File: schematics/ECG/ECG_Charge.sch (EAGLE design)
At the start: 8 parts, among them IC1 MCP73832_SOT23-5, J1 USB_MICROC

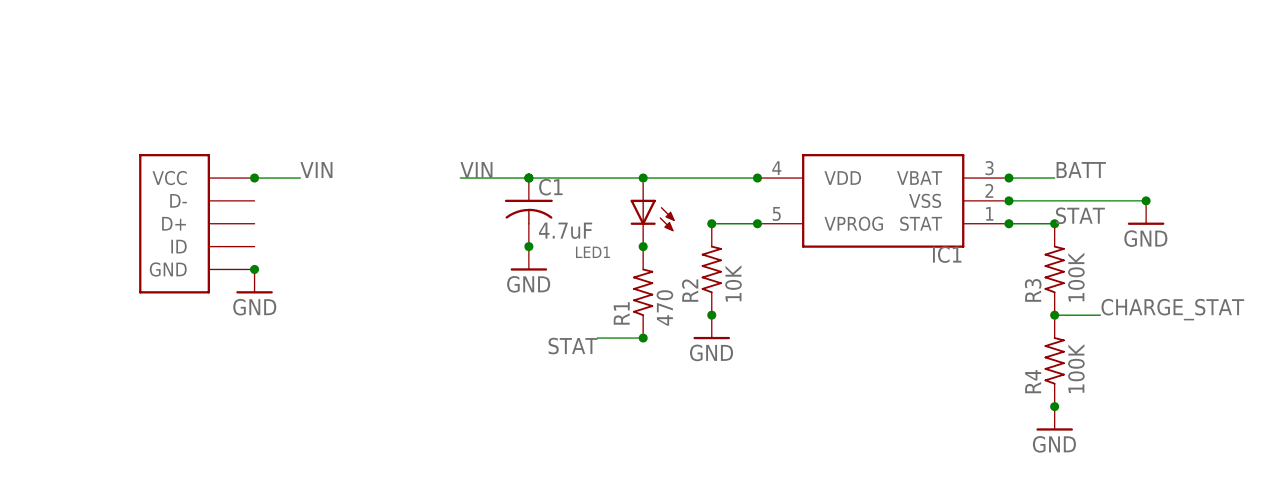
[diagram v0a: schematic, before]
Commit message: changed usb to micro usb, placed components in board area
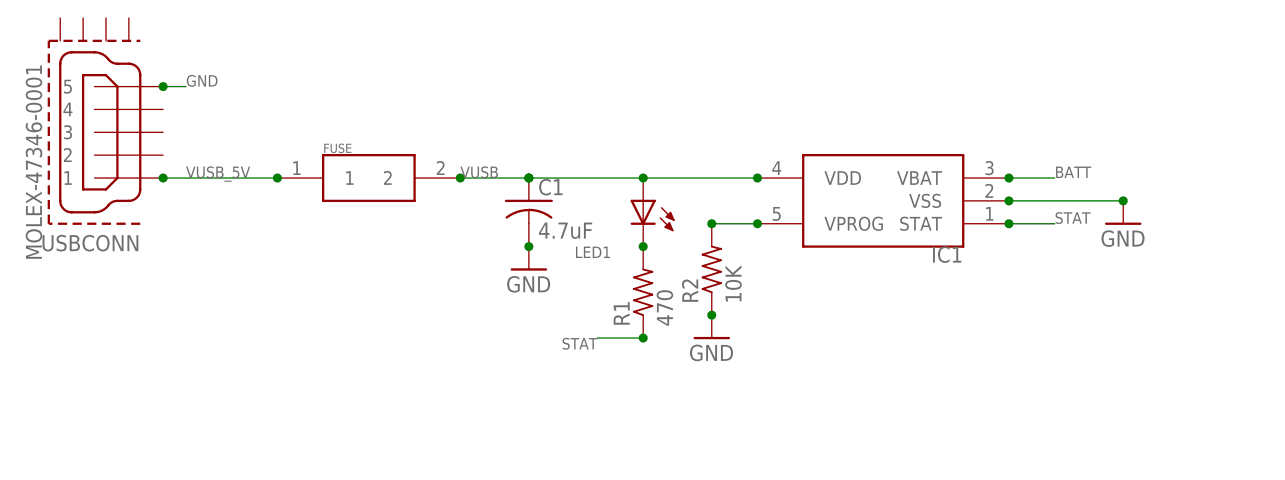
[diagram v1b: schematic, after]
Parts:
- removed J1: USB_MICROC, KomodoOpenLab:USB_MICROC
- removed R3, R4: 100K, rcl:R-US_R0201
- added FUSE: FUSE-MF_SERIES, bourns-fuse:FUSE-MF_SERIES
- added USBCONN: MOLEX-47346-0001, usb_con-update:MOLEX-47346-0001
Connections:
- removed net CHARGE_STAT: R3.1, R4.2
- removed net VIN: C1.1, IC1.VDD, J1.VCC, LED1.A
- new net VUSB: C1.1, FUSE.2, IC1.VDD, LED1.A
- new net VUSB_5V: FUSE.1, USBCONN.1
- net GND: now also USBCONN.5; no longer J1.GND, R4.1
- net STAT: no longer R3.2
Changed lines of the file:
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@@
 <parts>
 <part name="FRAME1" library="frames" deviceset="FRAME_A_L" device=""/>
-<part name="J1" library="KomodoOpenLab" deviceset="USB_MICROC" device=""/>
 <part name="IC1" library="KomodoOpenLab" deviceset="MCP73832_SOT23-5" device=""/>
 <part name="GND2" library="supply1" deviceset="GND" device=""/>
 <part name="R2" library="rcl" deviceset="R-US_" device="R0201" value="10K"/>
 <part name="GND3" library="supply1" deviceset="GND" device=""/>
-<part name="GND13" library="supply1" deviceset="GND" device=""/>
 <part name="C1" library="rcl" deviceset="C-US" device="C0402" value="4.7uF"/>
 <part name="GND19" library="supply1" deviceset="GND" device=""/>
-<part name="R3" library="rcl" deviceset="R-US_" device="R0201" value="100K"/>
-<part name="R4" library="rcl" deviceset="R-US_" device="R0201" value="100K"/>
-<part name="GND20" library="supply1" deviceset="GND" device=""/>
 <part name="LED1" library="LITEON" deviceset="LED_SMT_0805" device=""/>
 <part name="R1" library="rcl" deviceset="R-US_" device="R0201" value="470"/>
+<part name="USBCONN" library="usb_con-update" deviceset="MOLEX-47346-0001" device=""/>
+<part name="FUSE" library="bourns-fuse" deviceset="FUSE-MF_SERIES" device=""/>
 </parts>
 <sheets>
@@
 <instance part="FRAME1" gate="G$1" x="0" y="0"/>
 <instance part="FRAME1" gate="G$2" x="172.72" y="0"/>
-<instance part="J1" gate="G$1" x="144.78" y="66.04" rot="MR0"/>
 <instance part="IC1" gate="IC" x="220.98" y="73.66" rot="R180"/>
 <instance part="GND2" gate="1" x="180.34" y="66.04"/>
 <instance part="R2" gate="G$1" x="200.66" y="66.04" rot="R90"/>
 <instance part="GND3" gate="1" x="200.66" y="58.42"/>
-<instance part="GND13" gate="1" x="149.86" y="63.5" rot="MR0"/>
 <instance part="C1" gate="G$1" x="180.34" y="73.66"/>
-<instance part="GND19" gate="1" x="248.92" y="71.12"/>
-<instance part="R3" gate="G$1" x="238.76" y="66.04" rot="R90"/>
-<instance part="R4" gate="G$1" x="238.76" y="55.88" rot="R90"/>
-<instance part="GND20" gate="1" x="238.76" y="48.26"/>
+<instance part="GND19" gate="1" x="246.38" y="71.12"/>
 <instance part="LED1" gate="LED" x="193.04" y="73.66" rot="MR0"/>
 <instance part="R1" gate="G$1" x="193.04" y="63.5" rot="R90"/>
+<instance part="USBCONN" gate="G$1" x="134.62" y="81.28" rot="R180"/>
+<instance part="FUSE" gate="FUSE" x="162.56" y="76.2"/>
 </instances>
 <busses>
@@
 <nets>
 <net name="GND" class="0">
-<segment>
-<pinref part="J1" gate="G$1" pin="GND"/>
-<junction x="149.86" y="66.04"/>
-<pinref part="GND13" gate="1" pin="GND"/>
-</segment>
 <segment>
 <pinref part="GND2" gate="1" pin="GND"/>
@@
 <pinref part="IC1" gate="IC" pin="VSS"/>
 <junction x="233.68" y="73.66"/>
-<wire x1="233.68" y1="73.66" x2="248.92" y2="73.66" width="0.1524" layer="91"/>
+<wire x1="233.68" y1="73.66" x2="246.38" y2="73.66" width="0.1524" layer="91"/>
 <pinref part="GND19" gate="1" pin="GND"/>
-<junction x="248.92" y="73.66"/>
+<junction x="246.38" y="73.66"/>
 </segment>
 <segment>
-<pinref part="R4" gate="G$1" pin="1"/>
-<pinref part="GND20" gate="1" pin="GND"/>
-<junction x="238.76" y="50.8"/>
+<wire x1="139.7" y1="86.36" x2="142.24" y2="86.36" width="0.1524" layer="91"/>
+<junction x="139.7" y="86.36"/>
+<pinref part="USBCONN" gate="G$1" pin="5"/>
+<label x="142.24" y="86.36" size="1.27" layer="95"/>
 </segment>
 </net>
@@
 <junction x="233.68" y="71.12"/>
 <wire x1="233.68" y1="71.12" x2="238.76" y2="71.12" width="0.1524" layer="91"/>
-<label x="238.76" y="71.12" size="1.778" layer="95"/>
-<pinref part="R3" gate="G$1" pin="2"/>
-<junction x="238.76" y="71.12"/>
+<label x="238.76" y="71.12" size="1.27" layer="95"/>
 </segment>
 <segment>
@@
 <junction x="193.04" y="58.42"/>
 <wire x1="193.04" y1="58.42" x2="187.96" y2="58.42" width="0.1524" layer="91"/>
-<label x="187.96" y="58.42" size="1.778" layer="95" rot="R180"/>
+<label x="187.96" y="58.42" size="1.27" layer="95" rot="R180"/>
 </segment>
 </net>
@@
 </segment>
 </net>
-<net name="VIN" class="0">
-<segment>
-<pinref part="IC1" gate="IC" pin="VDD"/>
-<junction x="205.74" y="76.2"/>
-<wire x1="205.74" y1="76.2" x2="193.04" y2="76.2" width="0.1524" layer="91"/>
-<junction x="180.34" y="76.2"/>
-<wire x1="193.04" y1="76.2" x2="180.34" y2="76.2" width="0.1524" layer="91"/>
-<wire x1="180.34" y1="76.2" x2="172.72" y2="76.2" width="0.1524" layer="91"/>
-<label x="172.72" y="76.2" size="1.778" layer="95"/>
-<pinref part="C1" gate="G$1" pin="1"/>
-<junction x="180.34" y="76.2"/>
-<pinref part="LED1" gate="LED" pin="A"/>
-<junction x="193.04" y="76.2"/>
-</segment>
-<segment>
-<pinref part="J1" gate="G$1" pin="VCC"/>
-<junction x="149.86" y="76.2"/>
-<wire x1="149.86" y1="76.2" x2="154.94" y2="76.2" width="0.1524" layer="91"/>
-<label x="154.94" y="76.2" size="1.778" layer="95"/>
-</segment>
-</net>
 <net name="BATT" class="0">
 <segment>
@@
 <junction x="233.68" y="76.2"/>
 <wire x1="233.68" y1="76.2" x2="238.76" y2="76.2" width="0.1524" layer="91"/>
-<label x="238.76" y="76.2" size="1.778" layer="95"/>
-</segment>
-</net>
-<net name="CHARGE_STAT" class="0">
-<segment>
-<pinref part="R3" gate="G$1" pin="1"/>
-<pinref part="R4" gate="G$1" pin="2"/>
-<junction x="238.76" y="60.96"/>
-<wire x1="238.76" y1="60.96" x2="243.84" y2="60.96" width="0.1524" layer="91"/>
-<label x="243.84" y="60.96" size="1.778" layer="95"/>
+<label x="238.76" y="76.2" size="1.27" layer="95"/>
 </segment>
 </net>
@@
 </segment>
 </net>
+<net name="VUSB" class="0">
+<segment>
+<pinref part="IC1" gate="IC" pin="VDD"/>
+<junction x="205.74" y="76.2"/>
+<wire x1="205.74" y1="76.2" x2="193.04" y2="76.2" width="0.1524" layer="91"/>
+<junction x="180.34" y="76.2"/>
+<wire x1="193.04" y1="76.2" x2="180.34" y2="76.2" width="0.1524" layer="91"/>
+<wire x1="180.34" y1="76.2" x2="172.72" y2="76.2" width="0.1524" layer="91"/>
+<label x="172.72" y="76.2" size="1.27" layer="95"/>
+<pinref part="C1" gate="G$1" pin="1"/>
+<junction x="180.34" y="76.2"/>
+<pinref part="LED1" gate="LED" pin="A"/>
+<junction x="193.04" y="76.2"/>
+<pinref part="FUSE" gate="FUSE" pin="2"/>
+<junction x="172.72" y="76.2"/>
+</segment>
+</net>
+<net name="VUSB_5V" class="0">
+<segment>
+<wire x1="152.4" y1="76.2" x2="139.7" y2="76.2" width="0.1524" layer="91"/>
+<junction x="139.7" y="76.2"/>
+<junction x="152.4" y="76.2"/>
+<label x="142.24" y="76.2" size="1.27" layer="95"/>
+<pinref part="USBCONN" gate="G$1" pin="1"/>
+<pinref part="FUSE" gate="FUSE" pin="1"/>
+</segment>
+</net>
